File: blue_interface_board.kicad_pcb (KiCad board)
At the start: 4 copper layers, 92 x 73 mm, 98 parts, among them J1 Conn_01x05, J2 USB_B_Micro, J3 Conn_01x02, J4 Conn_01x02, J5 Conn_ARM_JTAG_SWD_10, J6 Conn_01x03, Q1 MMBT5401LT1G, Q2 Q_NMOS_GDS, Q3 MMBT3904, Q4 Q_NMOS_GDS, Q5 Q_NMOS_GDS, U1 93LCxxB, U2 FT232H, U3 ADM2682E, U4 TPD2E2U06, U5 TPD2E2U06, U6 LM5066, U7 STM32L011K4Tx, U9 MAXM15062, Y1 12MHz

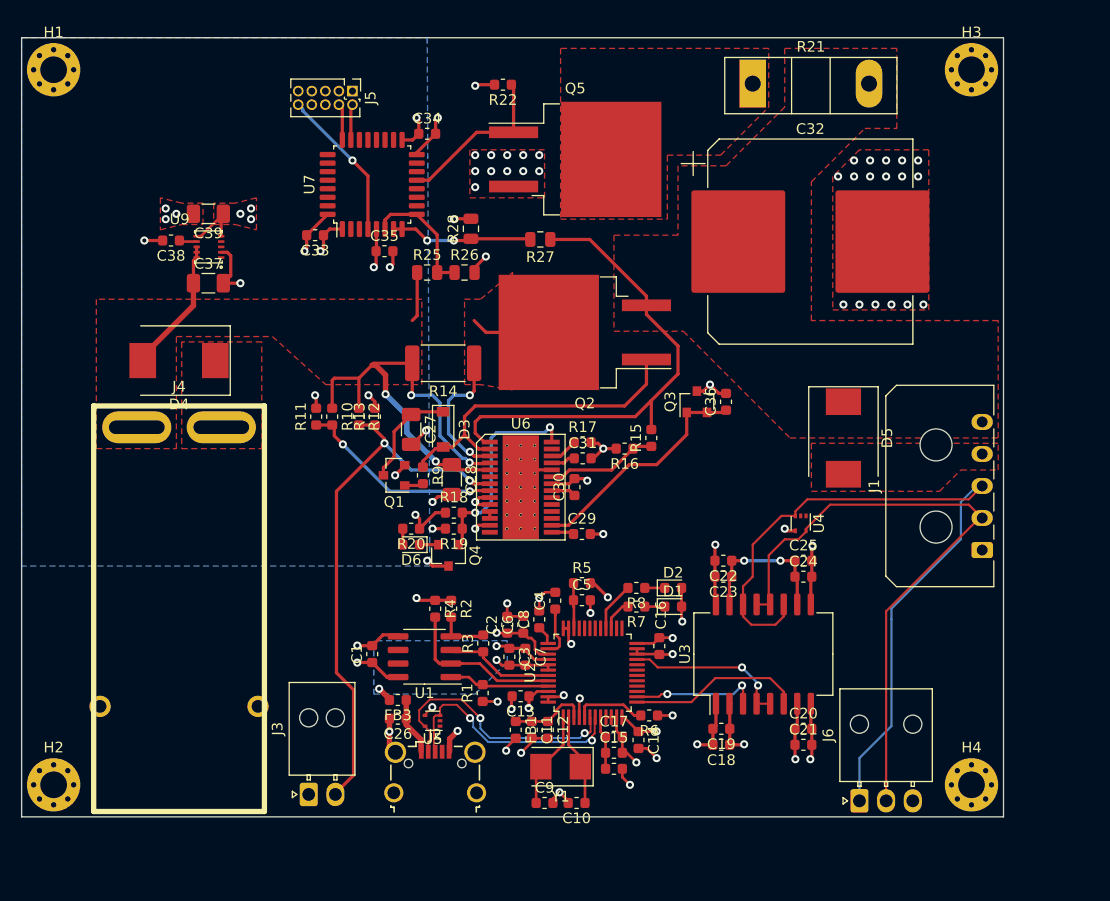
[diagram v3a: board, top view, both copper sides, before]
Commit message: Fixed flipped connector, changed most placement
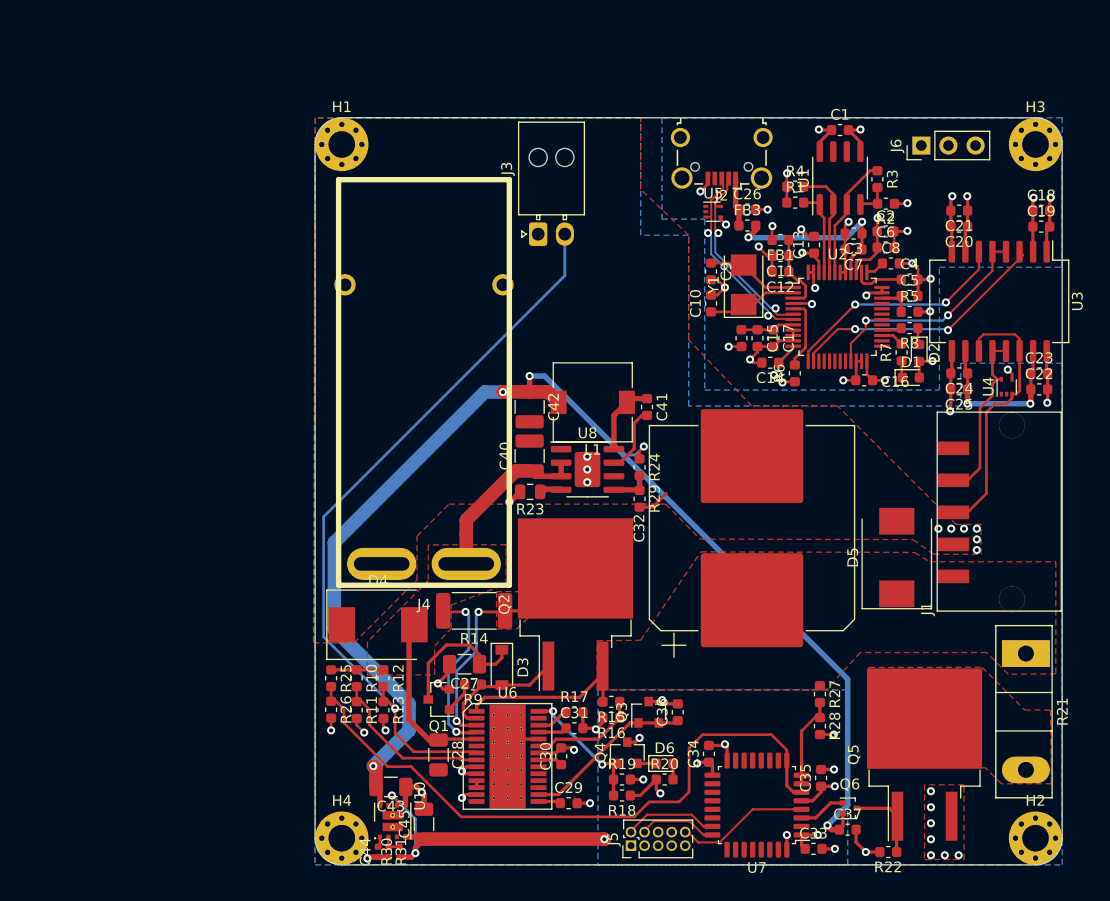
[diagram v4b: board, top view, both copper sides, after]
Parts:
- removed C38: 1u, Capacitor_SMD:C_0603_1608Metric
- removed C39: 10u, Capacitor_SMD:C_1206_3216Metric
- removed U9: MAXM15062, DCDC:MAXIM_uSLIP-10
- added C40: C_Small, Capacitor_SMD:C_1210_3225Metric, F.Cu at (109.1, 90.7)
- added C41: 2n2, Capacitor_SMD:C_0603_1608Metric, F.Cu at (120.1, 86.1)
- added C42: 22u, Capacitor_SMD:C_1210_3225Metric, F.Cu at (109.1, 86.1)
- added C43: 22u, Capacitor_SMD:C_1206_3216Metric, F.Cu at (96.1, 121.7)
- added C44: 4n7, Capacitor_SMD:C_0402_1005Metric, F.Cu at (94.9, 127.8)
- added C45: 47u, Capacitor_SMD:C_1206_3216Metric, F.Cu at (99.2, 125.2)
- added L1: 82u, Inductor_SMD:L_7.3x7.3_H4.5, F.Cu at (115.0, 85.7)
- added Q6: Q_NMOS_GDS, Package_TO_SOT_SMD:SOT-416, F.Cu at (139.1, 123.7)
- added R23: 40k2, Resistor_SMD:R_0805_2012Metric, F.Cu at (109.2, 94.0)
- added R24: 453k, Resistor_SMD:R_0603_1608Metric, F.Cu at (119.4, 91.8)
- added R29: 49k9, Resistor_SMD:R_0603_1608Metric, F.Cu at (119.4, 94.7)
- added R30: 562k, Resistor_SMD:R_0402_1005Metric, F.Cu at (96.9, 127.8)
- added R31: 180k, Resistor_SMD:R_0402_1005Metric, F.Cu at (95.9, 127.8)
- added U10: LMZ21700SIL, BLDC:SIL0008E, F.Cu at (96.3, 124.9)
- added U8: ti-LM5163, Package_SO:SOIC-8-1EP_3.9x4.9mm_P1.27mm_EP2.41x3.3mm, F.Cu at (114.5, 92.0)
- C37: value 1u -> 100n; footprint Capacitor_SMD:C_1206_3216Metric -> Capacitor_SMD:C_0603_1608Metric
- J1: footprint Connector_Molex:Molex_Micro-Fit_3.0_43650-0500_1x05_P3.00mm_Horizontal -> BLDC:molex-436500511
- J6: footprint Connector_Molex:Molex_Nano-Fit_105313-xx03_1x03_P2.50mm_Horizontal -> Connector_PinHeader_2.54mm:PinHeader_1x03_P2.54mm_Vertical
- R22: value 100k -> 1k
- R25, R26, R27, R28: footprint Resistor_SMD:R_0805_2012Metric -> Resistor_SMD:R_0603_1608Metric
- moved H2 92.1 mm to (156.5, 126.5)
- moved R22 80.5 mm to (142.7, 127.8)
- moved C37 78.8 mm to (138.9, 125.7)
- moved J5 75.4 mm to (118.6, 127.2), turned to 90 degrees
- moved C33 74.1 mm to (135.7, 127.5), turned to 0 degrees
- moved U7 68.4 mm to (130.4, 123.4), turned to 180 degrees
- moved C1 65.8 mm to (138.2, 60.1), turned to 0 degrees
- moved Q5 64.7 mm to (146.1, 118.7), turned to 90 degrees
- moved C35 64.1 mm to (136.4, 120.8), turned to 90 degrees
- moved C34 63.8 mm to (125.9, 118.6), turned to 90 degrees
- moved J2 63.5 mm to (127.1, 62.8), turned to 180 degrees
- moved J6 61.7 mm to (145.8, 61.6)
- moved U1 59.4 mm to (138.2, 64.7), turned to 90 degrees
- moved R21 59.2 mm to (155.6, 109.2), turned to 270 degrees
- moved H4 59.2 mm to (91.5, 126.5)
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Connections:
- C37 pad 1: /Power/VIN -> +12V
- R21 pad 1: Net-(Q5-Pad2) -> VOUT
- R21 pad 2: VOUT -> Net-(Q5-Pad2)
- U7 pad 13: Net-(Q5-Pad1) -> Net-(U7-Pad13)
- U7 pad 3: Net-(U7-Pad3) -> /Power/GATE_EN
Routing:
- net +12V: track 0.00 -> 120.5 mm, vias 0 -> 5
- net Net-(R25-Pad2): track 11.9 -> 60.6 mm
- net /Comms/RS485_A: track 71.3 -> 26.3 mm
- net /Comms/RS485_B: track 58.5 -> 16.9 mm
- net VOUT: track 46.3 -> 20.3 mm
- net +3.3VP: track 21.2 -> 43.9 mm
- net /Power/GATE: track 31.0 -> 11.8 mm
- net Net-(J3-Pad2): track 51.3 -> 70.1 mm, vias 2 -> 1
- net /Comms/RS485_RX: track 12.0 -> 24.7 mm
- net +5V: track 6.80 -> 17.8 mm
- net /Power/VIN: track 62.8 -> 54.4 mm, vias 4 -> 2
- net Net-(Q5-Pad1): track 15.5 -> 7.50 mm
- net Net-(C41-Pad1): track 0.00 -> 6.92 mm
- net /Power/PGD: track 19.6 -> 12.8 mm
- net Net-(C41-Pad2): track 0.00 -> 6.33 mm
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- added copper zone on B.Cu, net GNDD
- added copper zone on B.Cu, net GNDPWR
- removed copper zone on F.Cu, net +3.3VP
- removed copper zone on B.Cu, net +5V
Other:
- board size 92 x 73 mm -> 70 x 70 mm

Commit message: Fix DRCs and minor improvements
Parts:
- moved L1 0.37 mm to (115.0, 85.3)
- moved R29 0.10 mm to (119.4, 94.8)
- moved U8 0.07 mm to (114.6, 92.0)
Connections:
- H3 pad 1: GNDPWR -> Net-(H3-Pad1)
- J6 pad 1: /Comms/RS485_A -> /Comms/RS485_TX
- J6 pad 2: /Comms/RS485_B -> /Comms/RS485_RX
- J6 pad 3: GNDPWR -> GNDD
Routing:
- net /Comms/RS485_TX: track 21.7 -> 35.3 mm
- net /Comms/RS485_RX: track 24.7 -> 37.1 mm
- net GNDPWR: track 65.3 -> 70.8 mm
- net +12V: track 120.5 -> 121.3 mm

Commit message: Silk screen and cosmetic fixes
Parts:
- moved R1 2.18 mm to (133.0, 65.0)
- moved R4 2.18 mm to (133.0, 63.5)
- moved C1 0.90 mm to (137.3, 60.1)
- moved C11 0.90 mm to (131.7, 72.0)
- moved C12 0.90 mm to (131.7, 73.5)
- moved C13 0.90 mm to (134.8, 70.9)
- moved C14 0.90 mm to (130.8, 82.0)
- moved C18 0.90 mm to (156.1, 67.7)
- moved C19 0.90 mm to (156.1, 69.2)
- moved C20 0.90 mm to (148.4, 69.2)
- moved C21 0.90 mm to (148.4, 67.7)
- moved C22 0.90 mm to (155.9, 84.5)
- moved C23 0.90 mm to (155.9, 83.0)
- moved C24 0.90 mm to (148.4, 83.0)
- moved C25 0.90 mm to (148.4, 84.5)
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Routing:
- net /Comms/EECS: track 8.12 -> 9.94 mm
- net /Comms/EECLK: track 10.6 -> 11.7 mm
- net /Comms/RS485_A: track 26.3 -> 25.3 mm
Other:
- board text added: "GNDD"
- board text added: "RX"
- board text added: "TX"

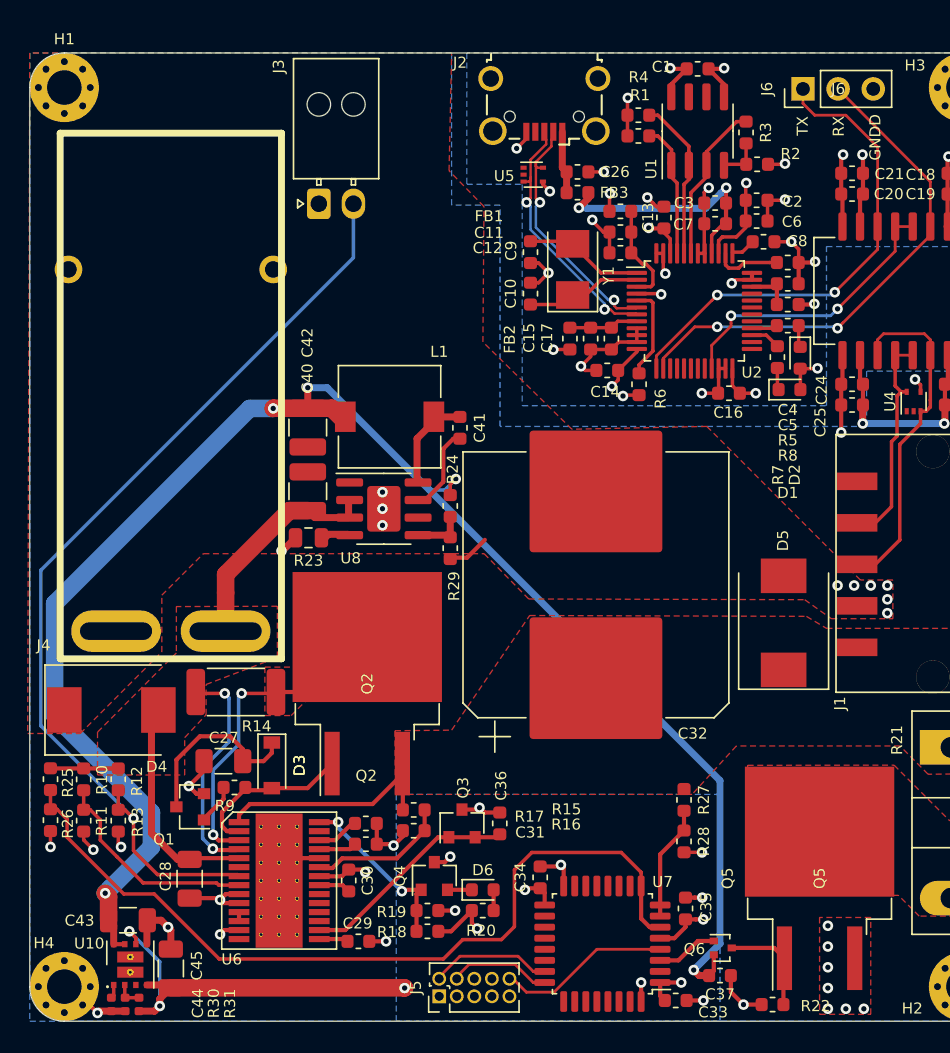
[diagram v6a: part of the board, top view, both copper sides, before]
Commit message: Changed voltage regulator, added I2C interface
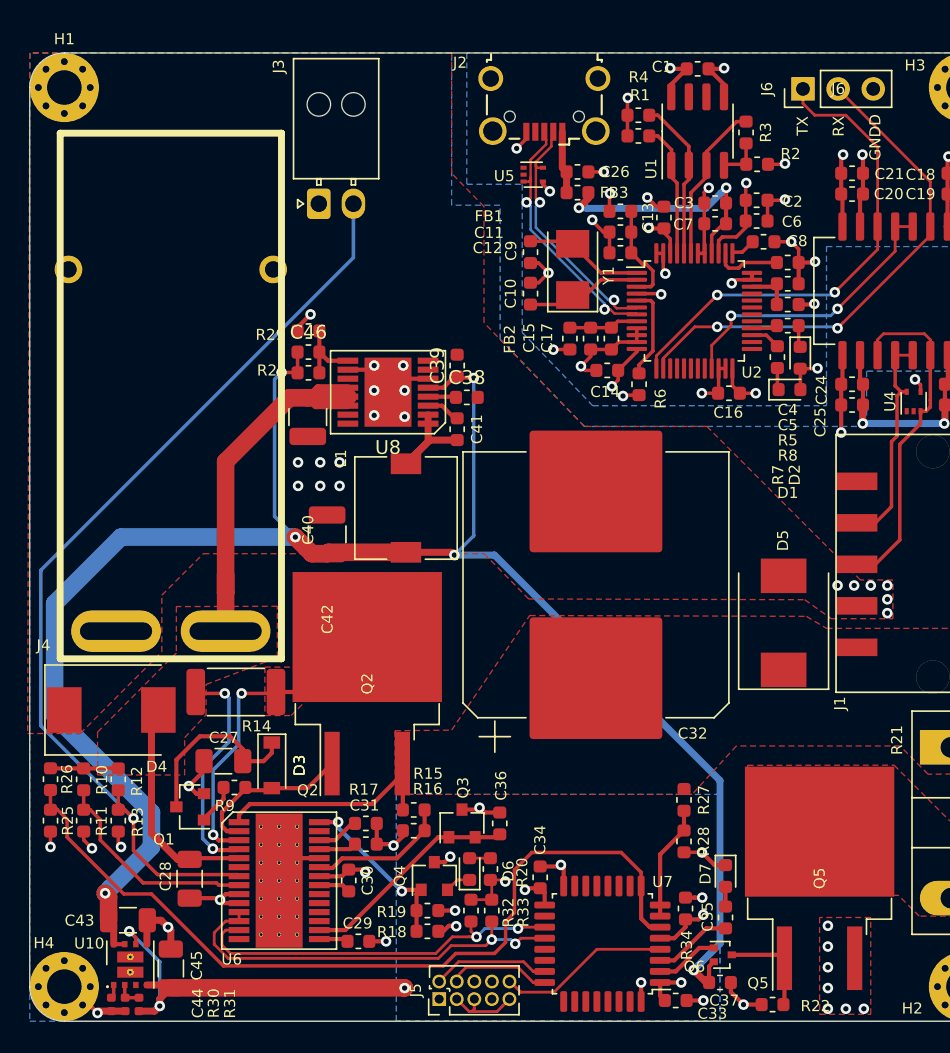
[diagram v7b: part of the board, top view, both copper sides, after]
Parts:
- removed R23: 40k2, Resistor_SMD:R_0805_2012Metric
- added C38: 2u2, Capacitor_SMD:C_0603_1608Metric, F.Cu at (120.6, 83.9)
- added C39: 2u2, Capacitor_SMD:C_0603_1608Metric, F.Cu at (119.9, 81.6)
- added C46: 82p, Capacitor_SMD:C_0603_1608Metric, F.Cu at (109.2, 80.6)
- added D7: LED, LED_SMD:LED_0603_1608Metric, F.Cu at (139.3, 118.5)
- added R32: 2.2k, Resistor_SMD:R_0603_1608Metric, F.Cu at (120.9, 121.0)
- added R33: 2.2k, Resistor_SMD:R_0603_1608Metric, F.Cu at (122.4, 121.0)
- added R34: 470R, Resistor_SMD:R_0603_1608Metric, F.Cu at (139.3, 121.5)
- C40: value C_Small -> 4u7
- C41: value 2n2 -> 470n
- L1: value 82u -> 100u
- R12: value 150k -> 140k
- R20: value 220R -> 470R
- R24: value 453k -> 1M
- R25: value 82.9k -> 6.65k
- R26: value 24.9k -> 140k
- R27: value 75k -> 140k
- R28: value 24.9k -> 6.34k
- R29: value 49k9 -> 91k
- U8: value ti-LM5163 -> LM46000; footprint Package_SO:SOIC-8-1EP_3.9x4.9mm_P1.27mm_EP2.41x3.3mm -> BLDC:PWP0016G
- moved R29 18.7 mm to (109.2, 79.1), turned to 180 degrees
- moved R24 14.1 mm to (109.2, 82.1), turned to 0 degrees
- moved U8 8.44 mm to (114.9, 83.5), turned to 90 degrees
- moved C42 7.84 mm to (110.5, 93.8), turned to 90 degrees
- moved L1 6.71 mm to (116.2, 91.9), turned to -90 degrees
- moved C40 5.36 mm to (109.1, 85.3), turned to -90 degrees
- moved R20 3.05 mm to (122.3, 118.0), turned to 90 degrees
- moved R25 3.00 mm to (90.5, 114.5)
- moved R26 2.96 mm to (90.5, 111.5)
- moved D6 1.78 mm to (120.8, 118.0), turned to 90 degrees
- moved C37 0.50 mm to (138.9, 126.2)
- moved Q6 0.50 mm to (139.1, 124.2)
- moved C41 0.22 mm to (119.9, 86.2)
- moved J5 0.20 mm to (118.6, 127.4)
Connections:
- L1 pad 1: Net-(C41-Pad1) -> Net-(C41-Pad2)
- R24 pad 2: Net-(R24-Pad2) -> Net-(C46-Pad2)
- R25 pad 1: /Power/VIN -> Net-(R25-Pad1)
- R25 pad 2: Net-(R25-Pad2) -> GNDPWR
- R26 pad 1: Net-(R25-Pad2) -> /Power/VIN
- R26 pad 2: GNDPWR -> Net-(R25-Pad1)
- R29 pad 1: Net-(R24-Pad2) -> Net-(C46-Pad2)
- U6 pad 11: Net-(U6-Pad11) -> /Power/SDA
- U6 pad 12: Net-(U6-Pad11) -> /Power/SDA
- U6 pad 13: GNDPWR -> /Power/SCL
- U7 pad 19: Net-(U7-Pad19) -> /Power/SCL
- U7 pad 2: Net-(U7-Pad2) -> /Power/GATE_EN
- U7 pad 20: Net-(U7-Pad20) -> /Power/SDA
- U7 pad 3: /Power/GATE_EN -> Net-(R34-Pad1)
- U7 pad 6: Net-(R25-Pad2) -> Net-(R25-Pad1)
- U7 pad 9: Net-(R25-Pad2) -> Net-(R25-Pad1)
- U8 pad 1: GNDPWR -> Net-(C41-Pad2)
- U8 pad 2: /Power/VIN -> Net-(C41-Pad2)
- U8 pad 3: /Power/VIN -> Net-(C41-Pad1)
- U8 pad 5: Net-(R24-Pad2) -> +12V
- U8 pad 6: Net-(U8-Pad6) -> GNDPWR
- U8 pad 7: Net-(C41-Pad2) -> Net-(U4-Pad7)
- U8 pad 8: Net-(C41-Pad1) -> Net-(U4-Pad8)
- U8 pad 9: GNDPWR -> Net-(C46-Pad2)
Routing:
- net Net-(R25-Pad1): track 0.00 -> 61.3 mm
- net Net-(R25-Pad2): track 60.6 -> 0.00 mm
- net /Power/SDA: track 0.00 -> 30.1 mm, vias 0 -> 2
- net /Power/SCL: track 0.00 -> 27.8 mm, vias 0 -> 2
- net +12V: track 121.3 -> 137.4 mm, vias 5 -> 6
- net /Power/VIN: track 54.4 -> 68.8 mm
- net GNDPWR: track 70.8 -> 79.0 mm, vias 40 -> 48
- net Net-(R34-Pad1): track 0.00 -> 5.68 mm
- net Net-(C46-Pad2): track 0.00 -> 5.27 mm
- net Net-(C41-Pad1): track 6.92 -> 2.48 mm
- net Net-(R24-Pad2): track 3.80 -> 0.00 mm
- net Net-(C41-Pad2): track 6.33 -> 8.62 mm
- net Net-(D7-Pad2): track 0.00 -> 1.43 mm
- net +3.3VP: track 43.9 -> 45.1 mm, vias 7 -> 8
- net Net-(U6-Pad11): track 0.65 -> 0.00 mm
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
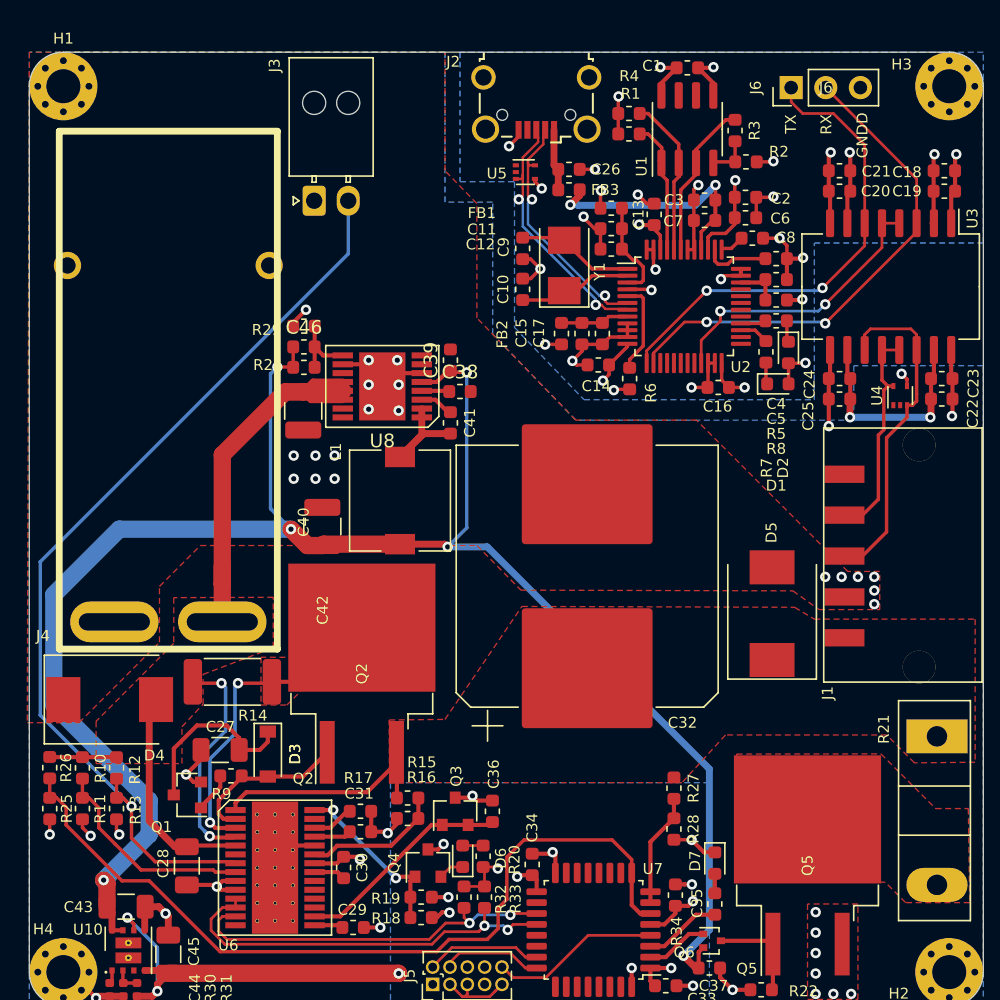
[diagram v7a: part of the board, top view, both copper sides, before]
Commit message: Changed connectors to microfit, added fan output
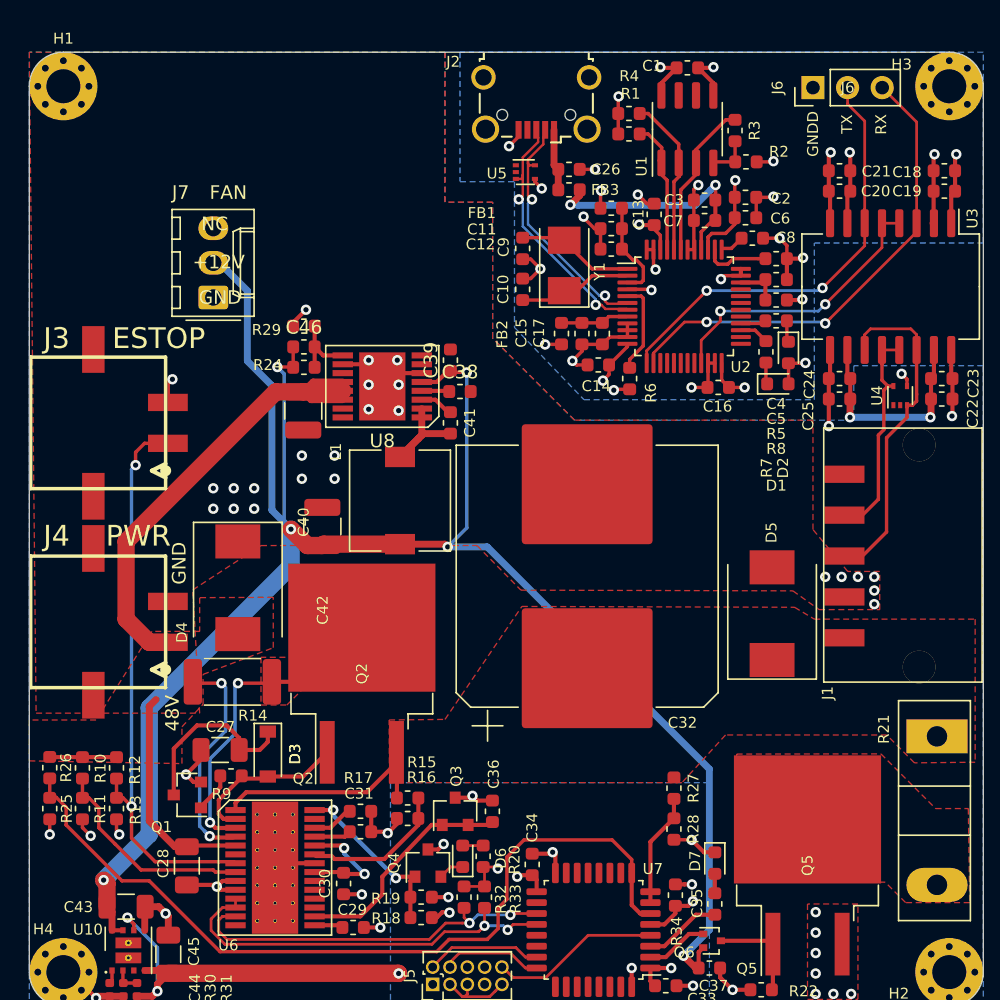
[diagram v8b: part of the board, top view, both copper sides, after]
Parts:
- added J7: FAN, Connector_Molex:Molex_KK-254_AE-6410-03A_1x03_P2.54mm_Vertical, F.Cu at (102.5, 77.0)
- J3: value Conn_01x02 -> ESTOP; footprint Connector_Molex:Molex_Nano-Fit_105313-xx02_1x02_P2.50mm_Horizontal -> BLDC:molex-0436500213
- J4: value Conn_01x02 -> PWR; footprint Connectors_OSRF:PP45_1X2 -> BLDC:molex-0436500213
- J6: value Conn_01x03 -> DNP
- R14: value 2m -> 15m
- R7, R8: value 220R -> 470R
- moved J3 26.4 mm to (89.1, 86.2), turned to -90 degrees
- moved D4 12.5 mm to (104.3, 98.3), turned to -90 degrees
- moved J4 10.1 mm to (89.1, 100.8), turned to -90 degrees
- moved J6 1.60 mm to (146.5, 61.6)
- moved C30 1.17 mm to (112.1, 120.0), turned to -90 degrees
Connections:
- C30 pad 1: Net-(C30-Pad1) -> /Power/LM_VDD
- J3 pad 1: GNDPWR -> Net-(J3-Pad1)
- J3 pad 2: Net-(J3-Pad2) -> GNDPWR
- J6 pad 1: /Comms/RS485_TX -> GNDD
- J6 pad 2: /Comms/RS485_RX -> /Comms/RS485_TX
- J6 pad 3: GNDD -> /Comms/RS485_RX
- R12 pad 2: Net-(J3-Pad2) -> Net-(J3-Pad1)
- R13 pad 1: Net-(J3-Pad2) -> Net-(J3-Pad1)
- U6 pad 21: Net-(C30-Pad1) -> /Power/LM_VDD
- U6 pad 24: GNDPWR -> /Power/LM_VDD
- U6 pad 7: Net-(J3-Pad2) -> Net-(J3-Pad1)
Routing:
- net Net-(J3-Pad2): track 70.1 -> 0.00 mm, vias 1 -> 0
- net Net-(J3-Pad1): track 0.00 -> 42.2 mm, vias 0 -> 2
- net +12V: track 137.4 -> 146.0 mm
- net /Power/LM_VDD: track 0.00 -> 8.50 mm, vias 0 -> 2
- net /Power/VIN: track 68.8 -> 74.3 mm
- net /Comms/RS485_TX: track 35.3 -> 32.2 mm
- net Net-(C30-Pad1): track 2.32 -> 0.00 mm
- net /Comms/RS485_RX: track 37.1 -> 35.4 mm
- net GNDPWR: track 79.0 -> 78.0 mm, vias 48 -> 53
- net Net-(C36-Pad1): track 15.9 -> 16.7 mm
- net Net-(R15-Pad1): track 10.3 -> 11.1 mm
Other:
- board text added: "+12V"
- board text added: "48V"
- board text added: "GND"
- board text added: "NC"
